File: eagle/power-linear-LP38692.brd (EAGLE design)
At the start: 32 x 24 mm, 13 parts, among them U1 LP38692

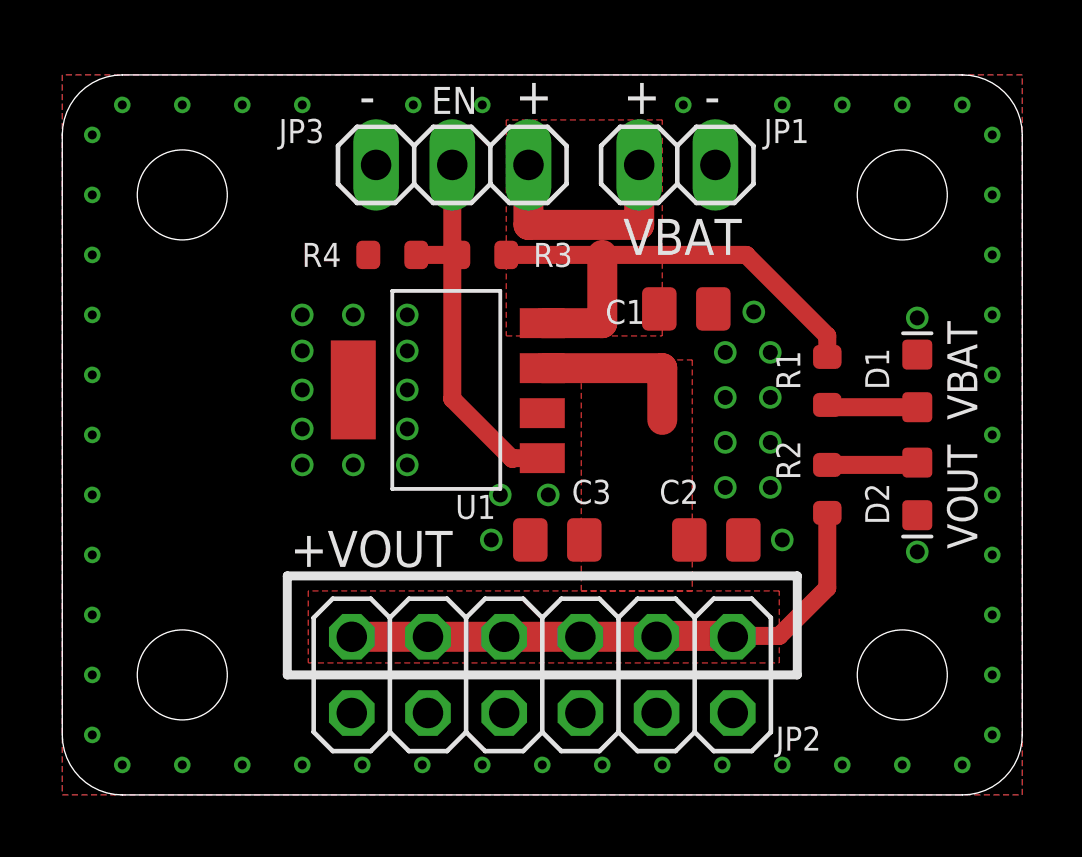
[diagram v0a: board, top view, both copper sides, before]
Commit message: Add adjust for LP38692
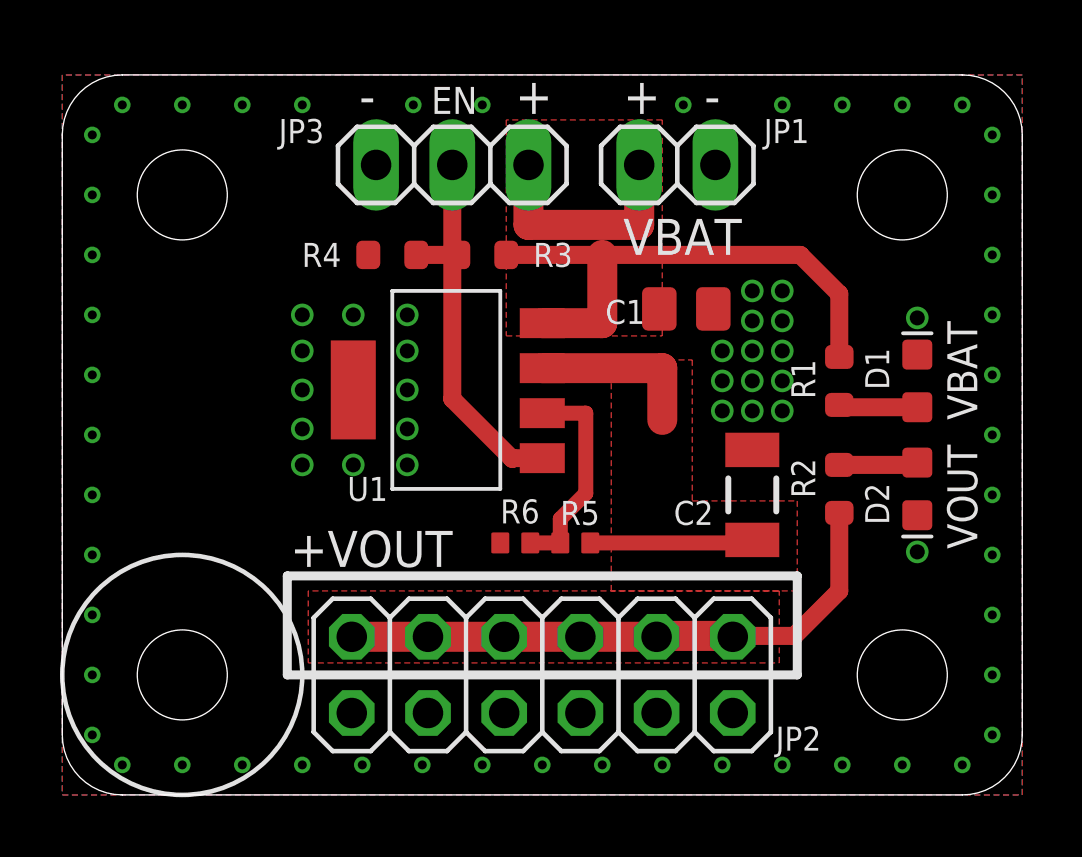
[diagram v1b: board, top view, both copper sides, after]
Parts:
- removed C3: NP, oresat-rcl:.0805-B-NOSILK
- added R5, R6: NP, oresat-rcl:.0402-B-NOSILK
- C2: device oresat-rcl:.0805-B-NOSILK -> oresat-rcl:1206-B
- moved C2 1.92 mm to (23.0, 10.0), turned to 90 degrees
- moved R1 0.40 mm to (25.9, 13.8)
- moved R2 0.40 mm to (25.9, 10.2)
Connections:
- new net N$1: R5.1, R6.2, U1.2
- net +VOUT: now also R5.2; no longer C3.1
- net GND: now also R6.1; no longer C3.2
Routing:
- net N$1: track 0.00 -> 7.13 mm
- net +VOUT: track 24.8 -> 30.7 mm
- net +VBAT: track 24.5 -> 25.7 mm
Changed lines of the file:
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@@
 2019-09-07  v1.0
 E.M. - KJ7AOG</text>
+<circle x="4" y="4" radius="4" width="0.1524" layer="21"/>
 </plain>
 <attributes>
@@
 <attribute name="NAME" x="20.8" y="16.2" size="0.3" layer="33" ratio="15" align="center"/>
 </element>
-<element name="C2" library="oresat-rcl" package=".0805-B-NOSILK" value="22u" x="21.8" y="8.5" smashed="yes">
-<attribute name="NAME" x="19.9" y="9.7" size="0.8" layer="25" font="vector" ratio="15"/>
-<attribute name="NAME" x="21.8" y="8.5" size="0.4" layer="33" ratio="15" align="center"/>
-</element>
-<element name="C3" library="oresat-rcl" package=".0805-B-NOSILK" value="NP" x="16.5" y="8.5" smashed="yes" rot="R180">
-<attribute name="NAME" x="18.3" y="10.5" size="0.8" layer="25" font="vector" ratio="15" rot="R180"/>
-<attribute name="NAME" x="16.5" y="8.5" size="0.4" layer="33" ratio="15" rot="R180" align="center"/>
+<element name="C2" library="oresat-rcl" package="1206-B" value="22u" x="23" y="10" smashed="yes" rot="R90">
+<attribute name="NAME" x="21.7" y="9.8" size="0.8" layer="25" font="vector" ratio="15" rot="R180"/>
+<attribute name="NAME" x="23" y="10" size="0.4" layer="33" ratio="15" rot="R90" align="center"/>
 </element>
 <element name="D2" library="SparkFun-LED" library_urn="urn:adsk.eagle:library:529" package="LED-0603" package3d_urn="urn:adsk.eagle:package:39354/1" value="GREEN" x="28.5" y="10.2" smashed="yes" rot="R270">
@@
 <attribute name="VALUE" x="9.19" y="17.825" size="1.27" layer="27"/>
 </element>
-<element name="R2" library="oresat-rcl" package=".0603-B-NOSILK" value="2.7k" x="25.5" y="10.2" smashed="yes" rot="R270">
-<attribute name="NAME" x="24.6" y="10.5" size="0.8" layer="25" font="vector" ratio="15" rot="R90"/>
-<attribute name="NAME" x="25.5" y="10.2" size="0.3" layer="33" ratio="15" rot="R270" align="center"/>
+<element name="R2" library="oresat-rcl" package=".0603-B-NOSILK" value="2.7k" x="25.9" y="10.2" smashed="yes" rot="R270">
+<attribute name="NAME" x="25.1" y="9.9" size="0.8" layer="25" font="vector" ratio="15" rot="R90"/>
+<attribute name="NAME" x="25.9" y="10.2" size="0.3" layer="33" ratio="15" rot="R270" align="center"/>
 </element>
 <element name="R4" library="oresat-rcl" package=".0603-B-NOSILK" value="NP" x="11" y="18" smashed="yes" rot="R180">
@@
 <attribute name="NAME" x="14" y="18" size="0.3" layer="33" ratio="15" rot="R180" align="center"/>
 </element>
-<element name="R1" library="oresat-rcl" package=".0603-B-NOSILK" value="5.6k" x="25.5" y="13.8" smashed="yes" rot="R90">
-<attribute name="NAME" x="24.6" y="13.5" size="0.8" layer="25" font="vector" ratio="15" rot="R90"/>
-<attribute name="NAME" x="25.5" y="13.8" size="0.3" layer="33" ratio="15" rot="R90" align="center"/>
+<element name="R1" library="oresat-rcl" package=".0603-B-NOSILK" value="5.6k" x="25.9" y="13.8" smashed="yes" rot="R90">
+<attribute name="NAME" x="25.1" y="13.2" size="0.8" layer="25" font="vector" ratio="15" rot="R90"/>
+<attribute name="NAME" x="25.9" y="13.8" size="0.3" layer="33" ratio="15" rot="R90" align="center"/>
 </element>
 <element name="U1" library="U-TI-LP38692-linear-reg" package="SOT223-5" value="LP38692" x="16" y="13.5" smashed="yes" rot="R90">
-<attribute name="NAME" x="13.1" y="9.2" size="0.8" layer="25" font="vector" ratio="15"/>
+<attribute name="NAME" x="9.5" y="9.8" size="0.8" layer="25" font="vector" ratio="15"/>
+</element>
+<element name="R5" library="oresat-rcl" package=".0402-B-NOSILK" value="NP" x="17.1" y="8.4" smashed="yes">
+<attribute name="NAME" x="16.6" y="9" size="0.8" layer="25" font="vector" ratio="15"/>
+<attribute name="NAME" x="17.1" y="8.4" size="0.3" layer="33" ratio="15" align="center"/>
+</element>
+<element name="R6" library="oresat-rcl" package=".0402-B-NOSILK" value="NP" x="15.1" y="8.4" smashed="yes">
+<attribute name="NAME" x="14.6" y="9.05" size="0.8" layer="25" font="vector" ratio="15"/>
+<attribute name="NAME" x="15.1" y="8.4" size="0.2" layer="33" ratio="15" align="center"/>
 </element>
 </elements>
@@
 <contactref element="JP1" pad="1"/>
 <contactref element="D2" pad="C"/>
-<contactref element="C3" pad="2"/>
 <contactref element="JP3" pad="1"/>
 <contactref element="R4" pad="2"/>
@@
 <via x="28.5" y="8.1" extent="1-16" drill="0.5"/>
 <via x="28.5" y="15.9" extent="1-16" drill="0.5"/>
-<via x="24" y="8.5" extent="1-16" drill="0.5"/>
-<via x="16.2" y="10" extent="1-16" drill="0.5"/>
-<via x="14.3" y="8.5" extent="1-16" drill="0.5"/>
-<via x="14.6" y="10" extent="1-16" drill="0.5"/>
 <via x="1" y="2" extent="1-16" drill="0.3"/>
 <via x="1" y="4" extent="1-16" drill="0.3"/>
@@
 <via x="1" y="12" extent="1-16" drill="0.3"/>
 <via x="1" y="10" extent="1-16" drill="0.3"/>
-<via x="22.1" y="10.25" extent="1-16" drill="0.5"/>
-<via x="22.1" y="11.75" extent="1-16" drill="0.5"/>
-<via x="22.1" y="13.25" extent="1-16" drill="0.5"/>
-<via x="22.1" y="14.75" extent="1-16" drill="0.5"/>
-<via x="23.6" y="10.25" extent="1-16" drill="0.5"/>
-<via x="23.6" y="11.75" extent="1-16" drill="0.5"/>
-<via x="23.6" y="13.25" extent="1-16" drill="0.5"/>
-<via x="23.6" y="14.75" extent="1-16" drill="0.5"/>
-<via x="23.05" y="16.1" extent="1-16" drill="0.5"/>
+<via x="22" y="12.8" extent="1-16" drill="0.5"/>
+<via x="23" y="12.8" extent="1-16" drill="0.5"/>
+<via x="24" y="12.8" extent="1-16" drill="0.5"/>
+<via x="22" y="13.8" extent="1-16" drill="0.5"/>
+<via x="23" y="13.8" extent="1-16" drill="0.5"/>
+<via x="24" y="13.8" extent="1-16" drill="0.5"/>
+<via x="23" y="14.8" extent="1-16" drill="0.5"/>
+<via x="24" y="14.8" extent="1-16" drill="0.5"/>
+<via x="24" y="15.8" extent="1-16" drill="0.5"/>
+<via x="23" y="15.8" extent="1-16" drill="0.5"/>
+<via x="23" y="16.8" extent="1-16" drill="0.5"/>
+<via x="22" y="14.8" extent="1-16" drill="0.5"/>
+<via x="24" y="16.8" extent="1-16" drill="0.5"/>
+<contactref element="R6" pad="1"/>
 </signal>
 <signal name="N$78">
 <contactref element="D2" pad="A"/>
 <contactref element="R2" pad="1"/>
-<wire x1="25.5" y1="11" x2="28.423" y2="11" width="0.6" layer="1"/>
+<wire x1="25.9" y1="11" x2="28.423" y2="11" width="0.6" layer="1"/>
 <wire x1="28.423" y1="11" x2="28.5" y2="11.077" width="0.6" layer="1"/>
 </signal>
@@
 <contactref element="D1" pad="A"/>
 <contactref element="R1" pad="1"/>
-<wire x1="25.5" y1="13" x2="25.577" y2="12.923" width="0.6" layer="1"/>
-<wire x1="25.577" y1="12.923" x2="28.5" y2="12.923" width="0.6" layer="1"/>
+<wire x1="25.9" y1="13" x2="25.977" y2="12.923" width="0.6" layer="1"/>
+<wire x1="25.977" y1="12.923" x2="28.5" y2="12.923" width="0.6" layer="1"/>
 </signal>
 <signal name="+VBAT">
@@
 <vertex x="20" y="22.5"/>
 </polygon>
-<wire x1="25.5" y1="14.6" x2="25.5" y2="15.3" width="0.6" layer="1"/>
-<wire x1="25.5" y1="15.3" x2="22.8" y2="18" width="0.6" layer="1"/>
-<wire x1="22.8" y1="18" x2="18" y2="18" width="0.6" layer="1"/>
+<wire x1="25.9" y1="14.6" x2="25.9" y2="16.7" width="0.6" layer="1"/>
+<wire x1="25.9" y1="16.7" x2="24.6" y2="18" width="0.6" layer="1"/>
+<wire x1="24.6" y1="18" x2="18" y2="18" width="0.6" layer="1"/>
 <wire x1="18" y1="18" x2="14.8" y2="18" width="0.6" layer="1"/>
 <wire x1="15.54" y1="21" x2="15.54" y2="19" width="1" layer="1"/>
@@
 <contactref element="JP2" pad="11"/>
 <contactref element="R2" pad="2"/>
-<contactref element="C3" pad="1"/>
 <polygon width="0.3" layer="1">
 <vertex x="8.2" y="4.4"/>
@@
 </polygon>
 <polygon width="0.3" layer="1">
-<vertex x="21" y="6.8"/>
-<vertex x="17.3" y="6.8"/>
-<vertex x="17.3" y="14.5"/>
+<vertex x="24.5" y="6.8"/>
+<vertex x="18.3" y="6.8"/>
+<vertex x="18.3" y="14.5"/>
 <vertex x="21" y="14.5"/>
+<vertex x="21" y="9.8"/>
+<vertex x="24.5" y="9.8"/>
 </polygon>
 <wire x1="16" y1="14.225" x2="20" y2="14.225" width="1" layer="1"/>
 <wire x1="20" y1="14.225" x2="20" y2="12.5" width="1" layer="1"/>
-<wire x1="25.5" y1="9.4" x2="25.5" y2="6.9" width="0.6" layer="1"/>
-<wire x1="25.5" y1="6.9" x2="23.9" y2="5.3" width="0.6" layer="1"/>
-<wire x1="23.9" y1="5.3" x2="22.38" y2="5.3" width="0.6" layer="1"/>
+<wire x1="25.9" y1="9.4" x2="25.9" y2="6.8" width="0.6" layer="1"/>
+<wire x1="25.9" y1="6.8" x2="24.4" y2="5.3" width="0.6" layer="1"/>
+<wire x1="24.4" y1="5.3" x2="22.38" y2="5.3" width="0.6" layer="1"/>
 <wire x1="22.38" y1="5.3" x2="22.35" y2="5.27" width="0.6" layer="1"/>
 <wire x1="9.65" y1="5.27" x2="12.19" y2="5.27" width="1" layer="1"/>
@@
 <wire x1="19.81" y1="5.27" x2="19.81" y2="5.3" width="1" layer="1"/>
 <wire x1="19.81" y1="5.3" x2="22.38" y2="5.3" width="1" layer="1"/>
+<contactref element="R5" pad="2"/>
+<wire x1="17.6" y1="8.4" x2="22.9" y2="8.4" width="0.5" layer="1"/>
+<wire x1="22.9" y1="8.4" x2="23" y2="8.5" width="0.5" layer="1"/>
+</signal>
+<signal name="N$1">
+<contactref element="R5" pad="1"/>
+<contactref element="R6" pad="2"/>
+<contactref element="U1" pad="2"/>
+<wire x1="16" y1="12.725" x2="17.45" y2="12.725" width="0.5" layer="1"/>
+<wire x1="17.45" y1="12.725" x2="17.45" y2="10.05" width="0.5" layer="1"/>
+<wire x1="17.45" y1="10.05" x2="16.6" y2="9.2" width="0.5" layer="1"/>
+<wire x1="16.6" y1="9.2" x2="16.6" y2="8.4" width="0.5" layer="1"/>
+<wire x1="15.6" y1="8.4" x2="16.6" y2="8.4" width="0.5" layer="1"/>
 </signal>
 </signals>
@@
 <mfgpreviewcolor name="substratecolor" color="0xFF786E46"/>
 </mfgpreviewcolors>
+<errors>
+</errors>
 </board>
 </drawing>

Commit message: Change res sizes for LP38692
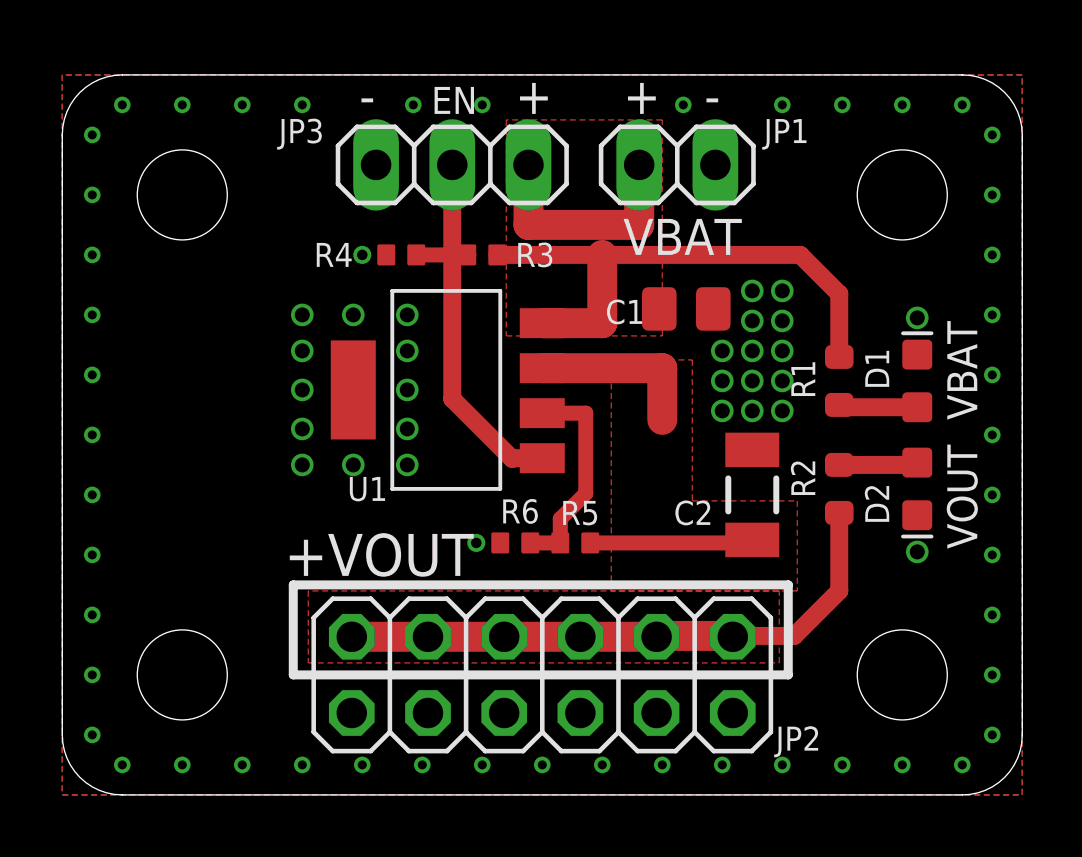
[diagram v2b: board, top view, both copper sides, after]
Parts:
- R3, R4: device oresat-rcl:.0603-B-NOSILK -> oresat-rcl:.0402-B-NOSILK
- moved R4 0.30 mm to (11.3, 18.0)
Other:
- board text added: "LDO Reg LP38692 fix/adj PSAS / OreSat 2019-09-08 v1.0 E.M. - KJ7AOG"
- board text removed: "LDO Reg LP38692 PSAS / OreSat 2019-09-07 v1.0 E.M. - KJ7AOG"
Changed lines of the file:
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@@
 <drawing>
 <settings>
-<setting alwaysvectorfont="no"/>
+<setting alwaysvectorfont="yes"/>
 <setting verticaltext="up"/>
 </settings>
@@
 <layer number="20" name="Dimension" color="24" fill="1" visible="yes" active="yes"/>
 <layer number="21" name="tPlace" color="7" fill="1" visible="yes" active="yes"/>
-<layer number="22" name="bPlace" color="7" fill="1" visible="yes" active="yes"/>
+<layer number="22" name="bPlace" color="7" fill="1" visible="no" active="yes"/>
 <layer number="23" name="tOrigins" color="15" fill="1" visible="yes" active="yes"/>
 <layer number="24" name="bOrigins" color="15" fill="1" visible="yes" active="yes"/>
@@
 <hole x="28" y="20" drill="3"/>
 <hole x="28" y="4" drill="3"/>
-<wire x1="7.5" y1="4" x2="24.5" y2="4" width="0.3" layer="21"/>
-<wire x1="24.5" y1="4" x2="24.5" y2="7.3" width="0.3" layer="21"/>
-<wire x1="24.5" y1="7.3" x2="7.5" y2="7.3" width="0.3" layer="21"/>
-<wire x1="7.5" y1="7.3" x2="7.5" y2="4" width="0.3" layer="21"/>
-<text x="7.6" y="7.6" size="1.2" layer="21" font="vector" ratio="15">+VOUT</text>
+<wire x1="7.7" y1="4" x2="24.2" y2="4" width="0.3" layer="21"/>
+<wire x1="24.2" y1="4" x2="24.2" y2="7" width="0.3" layer="21"/>
+<wire x1="24.2" y1="7" x2="7.7" y2="7" width="0.3" layer="21"/>
+<wire x1="7.7" y1="7" x2="7.7" y2="4" width="0.3" layer="21"/>
+<text x="7.4" y="7.3" size="1.4" layer="21" font="vector" ratio="15">+VOUT</text>
 <text x="18.7" y="18" size="1.2" layer="21" font="vector" ratio="15">VBAT</text>
 <text x="18.7" y="22.7" size="1.2" layer="21" font="vector" ratio="15">+</text>
@@
 <text x="9.9" y="22.7" size="1.2" layer="21" font="vector" ratio="15">-</text>
 <text x="21.4" y="22.7" size="1.2" layer="21" font="vector" ratio="15">-</text>
-<text x="22.5" y="12" size="1.2" layer="22" font="vector" ratio="15" rot="MR0">LDO Reg LP38692
+<text x="7.2" y="13.9" size="1.2" layer="22" font="vector" ratio="15" rot="SMR180">LDO Reg LP38692 fix/adj
 PSAS / OreSat
-2019-09-07  v1.0
+2019-09-08  v1.0
 E.M. - KJ7AOG</text>
-<circle x="4" y="4" radius="4" width="0.1524" layer="21"/>
 </plain>
 <attributes>
@@
 <attribute name="NAME" x="25.9" y="10.2" size="0.3" layer="33" ratio="15" rot="R270" align="center"/>
 </element>
-<element name="R4" library="oresat-rcl" package=".0603-B-NOSILK" value="NP" x="11" y="18" smashed="yes" rot="R180">
-<attribute name="NAME" x="9.3" y="18.4" size="0.8" layer="25" font="vector" ratio="15" rot="R180"/>
-<attribute name="NAME" x="11" y="18" size="0.3" layer="33" ratio="15" rot="R180" align="center"/>
-</element>
-<element name="R3" library="oresat-rcl" package=".0603-B-NOSILK" value="NP" x="14" y="18" smashed="yes" rot="R180">
-<attribute name="NAME" x="15.7" y="17.6" size="0.8" layer="25" font="vector" ratio="15"/>
+<element name="R4" library="oresat-rcl" package=".0402-B-NOSILK" value="NP" x="11.3" y="18" smashed="yes" rot="R180">
+<attribute name="NAME" x="9.7" y="18.4" size="0.8" layer="25" font="vector" ratio="15" rot="R180"/>
+<attribute name="NAME" x="11.3" y="18" size="0.3" layer="33" ratio="15" rot="R180" align="center"/>
+</element>
+<element name="R3" library="oresat-rcl" package=".0402-B-NOSILK" value="NP" x="14" y="18" smashed="yes" rot="R180">
+<attribute name="NAME" x="15.1" y="17.6" size="0.8" layer="25" font="vector" ratio="15"/>
 <attribute name="NAME" x="14" y="18" size="0.3" layer="33" ratio="15" rot="R180" align="center"/>
 </element>
@@
 <via x="24" y="16.8" extent="1-16" drill="0.5"/>
 <contactref element="R6" pad="1"/>
+<via x="10" y="18" extent="1-16" drill="0.35"/>
+<via x="13.8" y="8.4" extent="1-16" drill="0.35"/>
 </signal>
 <signal name="N$78">
@@
 <wire x1="15" y1="11.2" x2="15.025" y2="11.225" width="0.6" layer="1"/>
 <wire x1="15.025" y1="11.225" x2="16" y2="11.225" width="0.6" layer="1"/>
-<wire x1="11.8" y1="18" x2="13" y2="18" width="0.6" layer="1"/>
-<wire x1="13.2" y1="18" x2="13" y2="18" width="0.6" layer="1"/>
+<wire x1="13.5" y1="18" x2="13" y2="18" width="0.6" layer="1"/>
+<wire x1="11.8" y1="18" x2="13" y2="18" width="0.5" layer="1"/>
 </signal>
 <signal name="N$4">
@@
 <wire x1="25.9" y1="16.7" x2="24.6" y2="18" width="0.6" layer="1"/>
 <wire x1="24.6" y1="18" x2="18" y2="18" width="0.6" layer="1"/>
-<wire x1="18" y1="18" x2="14.8" y2="18" width="0.6" layer="1"/>
+<wire x1="18" y1="18" x2="14.5" y2="18" width="0.6" layer="1"/>
 <wire x1="15.54" y1="21" x2="15.54" y2="19" width="1" layer="1"/>
 <wire x1="19.23" y1="19" x2="19.23" y2="21" width="1" layer="1"/>
